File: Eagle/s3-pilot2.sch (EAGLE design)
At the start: 17 parts, among them J1 ARDUINO_R3_SHIELD, M2_1 ENA_JMP

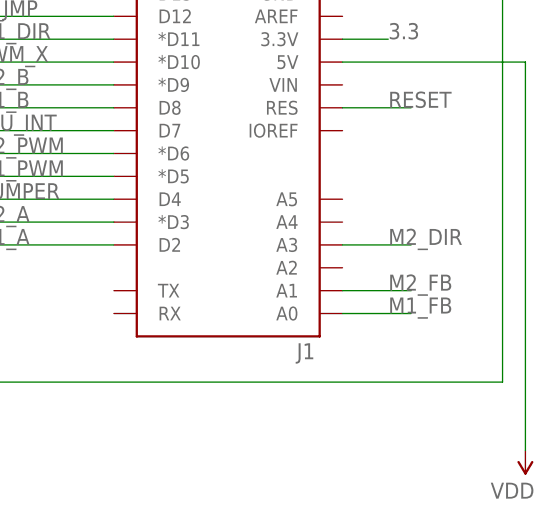
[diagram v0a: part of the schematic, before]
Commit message: work session with David verified ESC work - problem was buttons on breadboard verify a few updates and eagle, then re-order Code needs to be split / merged / something to deal with various situations need 2-way serial now, since cant really use breadboard buttons anymore.
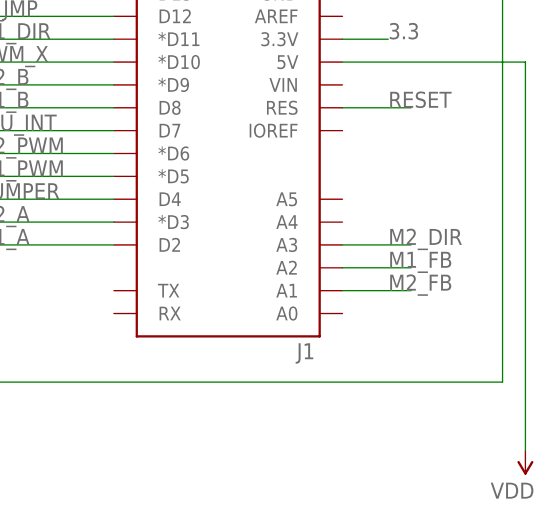
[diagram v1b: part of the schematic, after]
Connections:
- net M1_FB: now also J1.A2; no longer J1.A0
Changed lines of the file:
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@@
 <net name="M1_FB" class="0">
-<segment>
-<pinref part="J1" gate="G$1" pin="A0"/>
-<wire x1="223.52" y1="45.72" x2="231.14" y2="45.72" width="0.1524" layer="91"/>
-<label x="228.6" y="45.72" size="1.778" layer="95"/>
-</segment>
 <segment>
 <pinref part="U$1" gate="G$1" pin="FB"/>
@@
 <label x="63.5" y="99.06" size="1.778" layer="95"/>
 </segment>
+<segment>
+<pinref part="J1" gate="G$1" pin="A2"/>
+<wire x1="223.52" y1="50.8" x2="231.14" y2="50.8" width="0.1524" layer="91"/>
+<label x="228.6" y="50.8" size="1.778" layer="95"/>
+</segment>
 </net>
